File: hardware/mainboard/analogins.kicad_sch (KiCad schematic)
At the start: 27 parts, among them J3 CASTOR PITCH, J4 POLLUX PITCH, J5 CASTOR DUTY, J6 POLLUX DUTY, U6 MCP6004

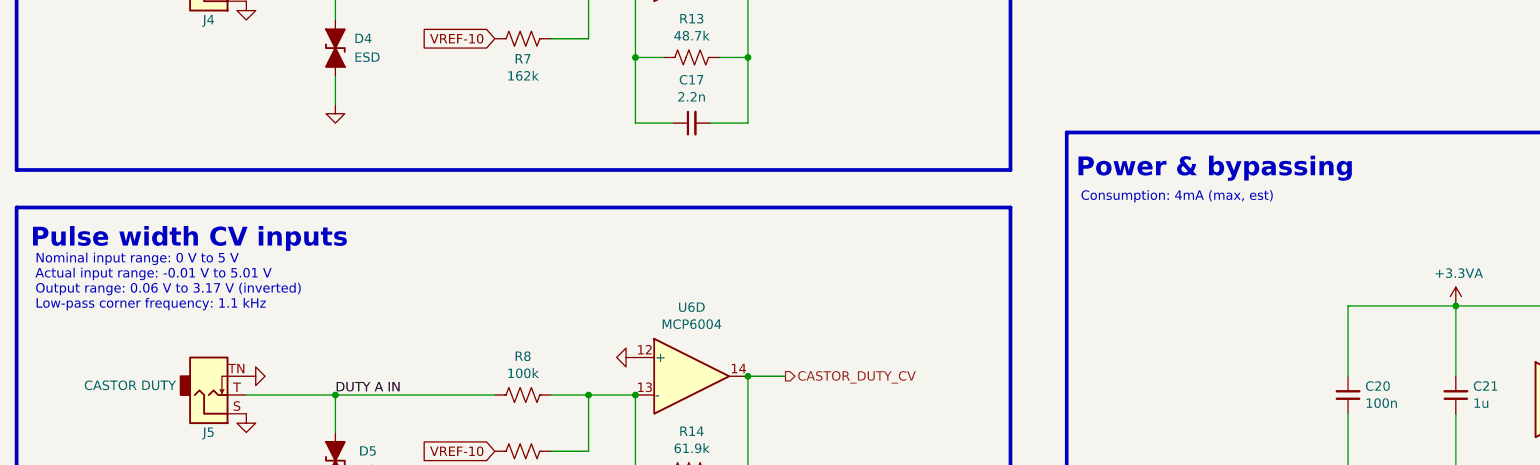
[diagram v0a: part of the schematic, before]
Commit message: A little more schematic cleanup
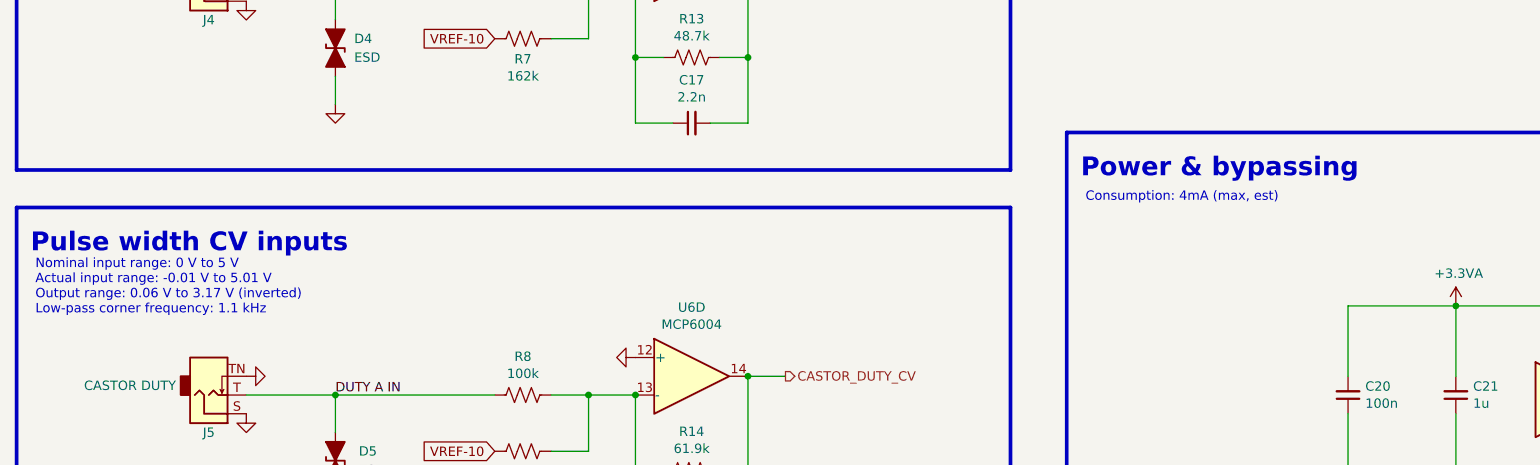
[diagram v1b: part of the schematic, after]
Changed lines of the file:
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@@
     (stroke (width 0) (type default) (color 0 0 0 0))
   )
-  (text "Pulse width CV inputs" (at 19.685 114.935 0)
+  (text "Pulse width CV inputs" (at 19.685 115.57 0)
     (effects (font (size 2.54 2.54) (thickness 0.508) bold) (justify left bottom))
   )
-  (text "Consumption: 4mA (max, est)" (at 161.925 108.585 0)
+  (text "Consumption: 4mA (max, est)" (at 162.56 108.585 0)
     (effects (font (size 1.27 1.27)) (justify left bottom))
   )
-  (text "Power & bypassing" (at 161.29 105.41 0)
+  (text "Power & bypassing" (at 161.925 105.41 0)
     (effects (font (size 2.54 2.54) (thickness 0.508) bold) (justify left bottom))
   )
@@
   )
   (text "Nominal input range: 0 V to 5 V\nActual input range: -0.01 V to 5.01 V\nOutput range: 0.06 V to 3.17 V (inverted)\nLow-pass corner frequency: 1.1 kHz\n"
-    (at 20.32 123.19 0)
+    (at 20.32 123.825 0)
     (effects (font (size 1.27 1.27)) (justify left bottom))
   )

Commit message: Finalize resistor mpns
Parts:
- R10, R4, R6, R8: mpn (none) -> RC0402DR-07100KL
- R11, R9: mpn (none) -> RP73PF1E196KBTD, RK73H1ETTP1963F
- R12, R13: mpn (none) -> RT0402BRD0748K7L
- R14, R15: mpn (none) -> RT0402BRD0761K9L, ERA-2AEB6192X
- R5, R7: mpn (none) -> RP73PF1E162KBTD
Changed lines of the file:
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@@
       (effects (font (size 1.27 1.27)) hide)
     )
-    (property "mpn" "" (id 5) (at 86.36 40.64 0)
+    (property "mpn" "RC0402DR-07100KL" (id 5) (at 86.36 40.64 0)
       (effects (font (size 1.27 1.27)) hide)
     )
@@
       (effects (font (size 1.27 1.27)) hide)
     )
-    (property "mpn" "" (id 5) (at 86.36 48.26 0)
+    (property "mpn" "RP73PF1E162KBTD" (id 5) (at 86.36 48.26 0)
       (effects (font (size 1.27 1.27)) hide)
     )
@@
       (effects (font (size 1.27 1.27)) hide)
     )
-    (property "mpn" "" (id 5) (at 109.22 50.8 0)
+    (property "mpn" "RT0402BRD0748K7L" (id 5) (at 109.22 50.8 0)
       (effects (font (size 1.27 1.27)) hide)
     )
@@
       (effects (font (size 1.27 1.27)) hide)
     )
-    (property "mpn" "" (id 5) (at 86.36 78.74 0)
+    (property "mpn" "RC0402DR-07100KL" (id 5) (at 86.36 78.74 0)
       (effects (font (size 1.27 1.27)) hide)
     )
@@
       (effects (font (size 1.27 1.27)) hide)
     )
-    (property "mpn" "" (id 5) (at 86.36 86.36 0)
+    (property "mpn" "RP73PF1E162KBTD" (id 5) (at 86.36 86.36 0)
       (effects (font (size 1.27 1.27)) hide)
     )
@@
       (effects (font (size 1.27 1.27)) hide)
     )
-    (property "mpn" "" (id 5) (at 109.22 88.9 0)
+    (property "mpn" "RT0402BRD0748K7L" (id 5) (at 109.22 88.9 0)
       (effects (font (size 1.27 1.27)) hide)
     )
@@
       (effects (font (size 1.27 1.27)) hide)
     )
-    (property "mpn" "" (id 5) (at 86.36 134.62 0)
+    (property "mpn" "RC0402DR-07100KL" (id 5) (at 86.36 134.62 0)
       (effects (font (size 1.27 1.27)) hide)
     )
@@
       (effects (font (size 1.27 1.27)) hide)
     )
-    (property "mpn" "" (id 5) (at 86.36 142.24 0)
+    (property "mpn" " RP73PF1E196KBTD, RK73H1ETTP1963F" (id 5) (at 86.36 142.24 0)
       (effects (font (size 1.27 1.27)) hide)
     )
@@
       (effects (font (size 1.27 1.27)) hide)
     )
-    (property "mpn" "" (id 5) (at 109.22 144.78 0)
+    (property "mpn" "RT0402BRD0761K9L,  ERA-2AEB6192X" (id 5) (at 109.22 144.78 0)
       (effects (font (size 1.27 1.27)) hide)
     )
@@
       (effects (font (size 1.27 1.27)) hide)
     )
-    (property "mpn" "" (id 5) (at 86.36 171.45 0)
+    (property "mpn" "RC0402DR-07100KL" (id 5) (at 86.36 171.45 0)
       (effects (font (size 1.27 1.27)) hide)
     )
@@
       (effects (font (size 1.27 1.27)) hide)
     )
-    (property "mpn" "" (id 5) (at 86.36 179.07 0)
+    (property "mpn" " RP73PF1E196KBTD, RK73H1ETTP1963F" (id 5) (at 86.36 179.07 0)
       (effects (font (size 1.27 1.27)) hide)
     )
@@
       (effects (font (size 1.27 1.27)) hide)
     )
-    (property "mpn" "" (id 5) (at 109.22 181.61 0)
-      (effects (font (size 1.27 1.27)) hide)
-    )
+    (property "mpn" "RT0402BRD0761K9L,  ERA-2AEB6192X" (id 5) (at 109.22 181.61 0)
+      (effects (font (size 1.27 1.27)) hide)
+    )

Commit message: Update some MPNs
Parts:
- R11, R9: mpn RP73PF1E196KBTD, RK73H1ETTP1963F -> RP73PF1E196KBTD, RK73H1ETTP1963F
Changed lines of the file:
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@@
       (effects (font (size 1.27 1.27)) hide)
     )
-    (property "mpn" " RP73PF1E196KBTD, RK73H1ETTP1963F" (id 5) (at 86.36 142.24 0)
+    (property "mpn" "RP73PF1E196KBTD, RK73H1ETTP1963F" (id 5) (at 86.36 142.24 0)
       (effects (font (size 1.27 1.27)) hide)
     )
@@
       (effects (font (size 1.27 1.27)) hide)
     )
-    (property "mpn" " RP73PF1E196KBTD, RK73H1ETTP1963F" (id 5) (at 86.36 179.07 0)
+    (property "mpn" "RP73PF1E196KBTD, RK73H1ETTP1963F" (id 5) (at 86.36 179.07 0)
       (effects (font (size 1.27 1.27)) hide)
     )

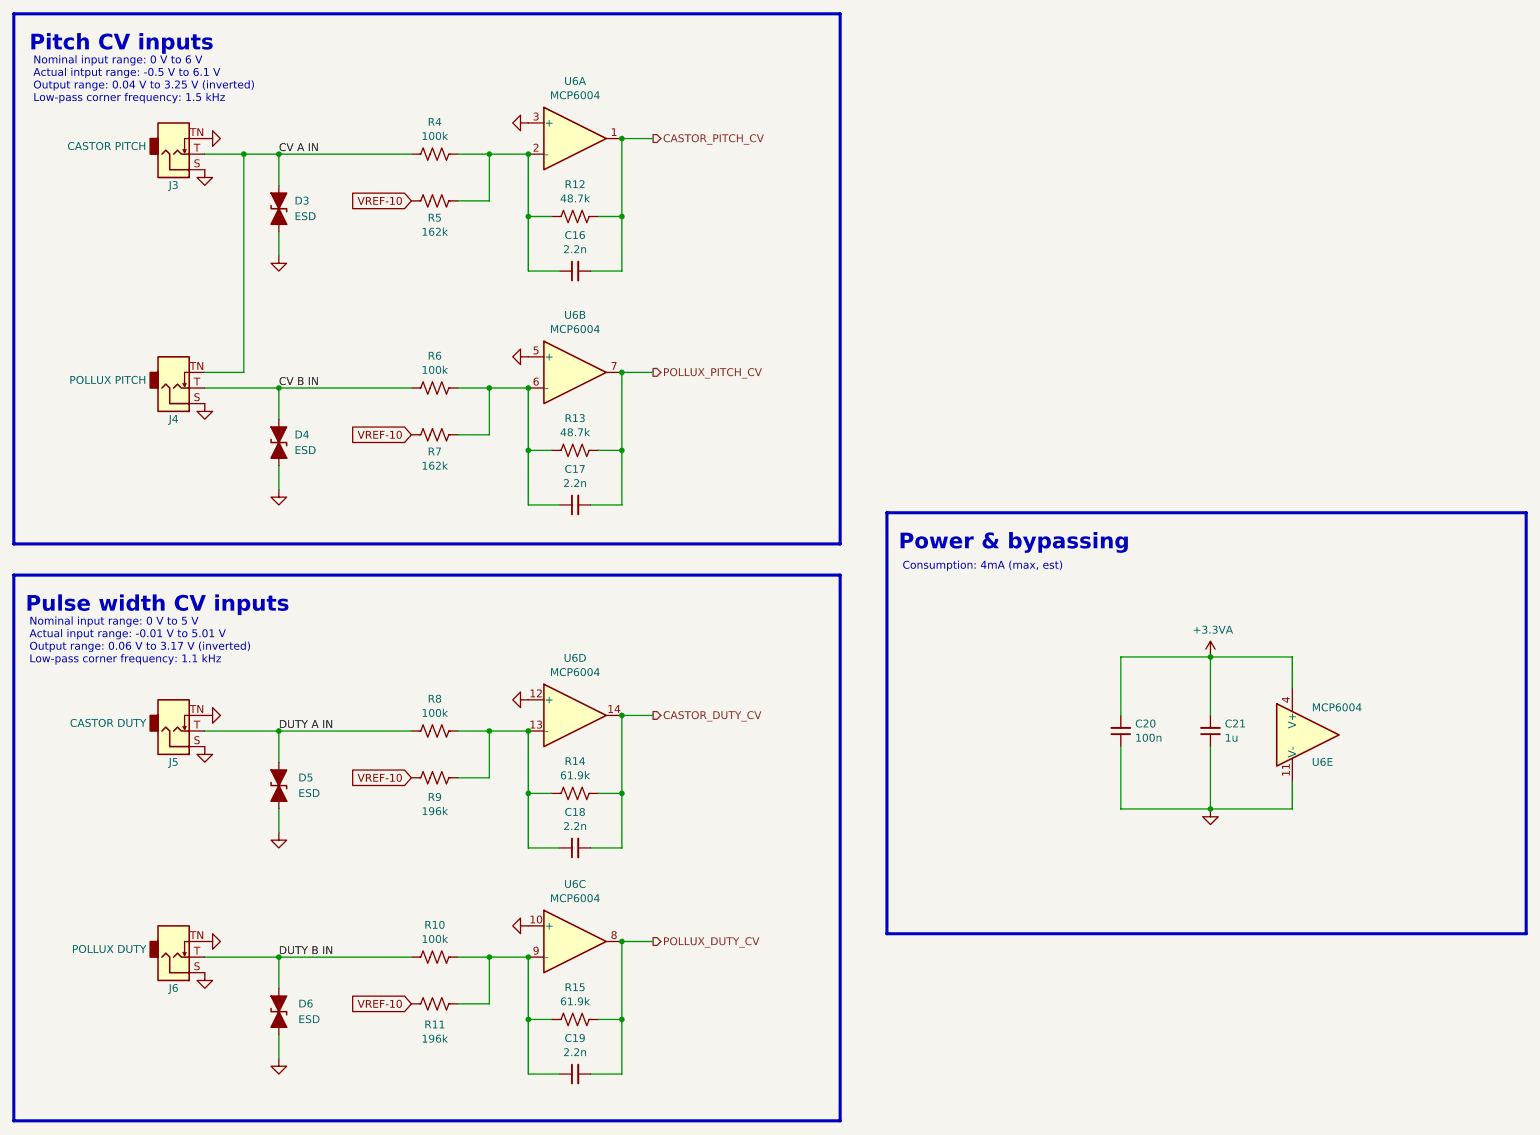
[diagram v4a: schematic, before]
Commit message: hardware: add rating field to schematic
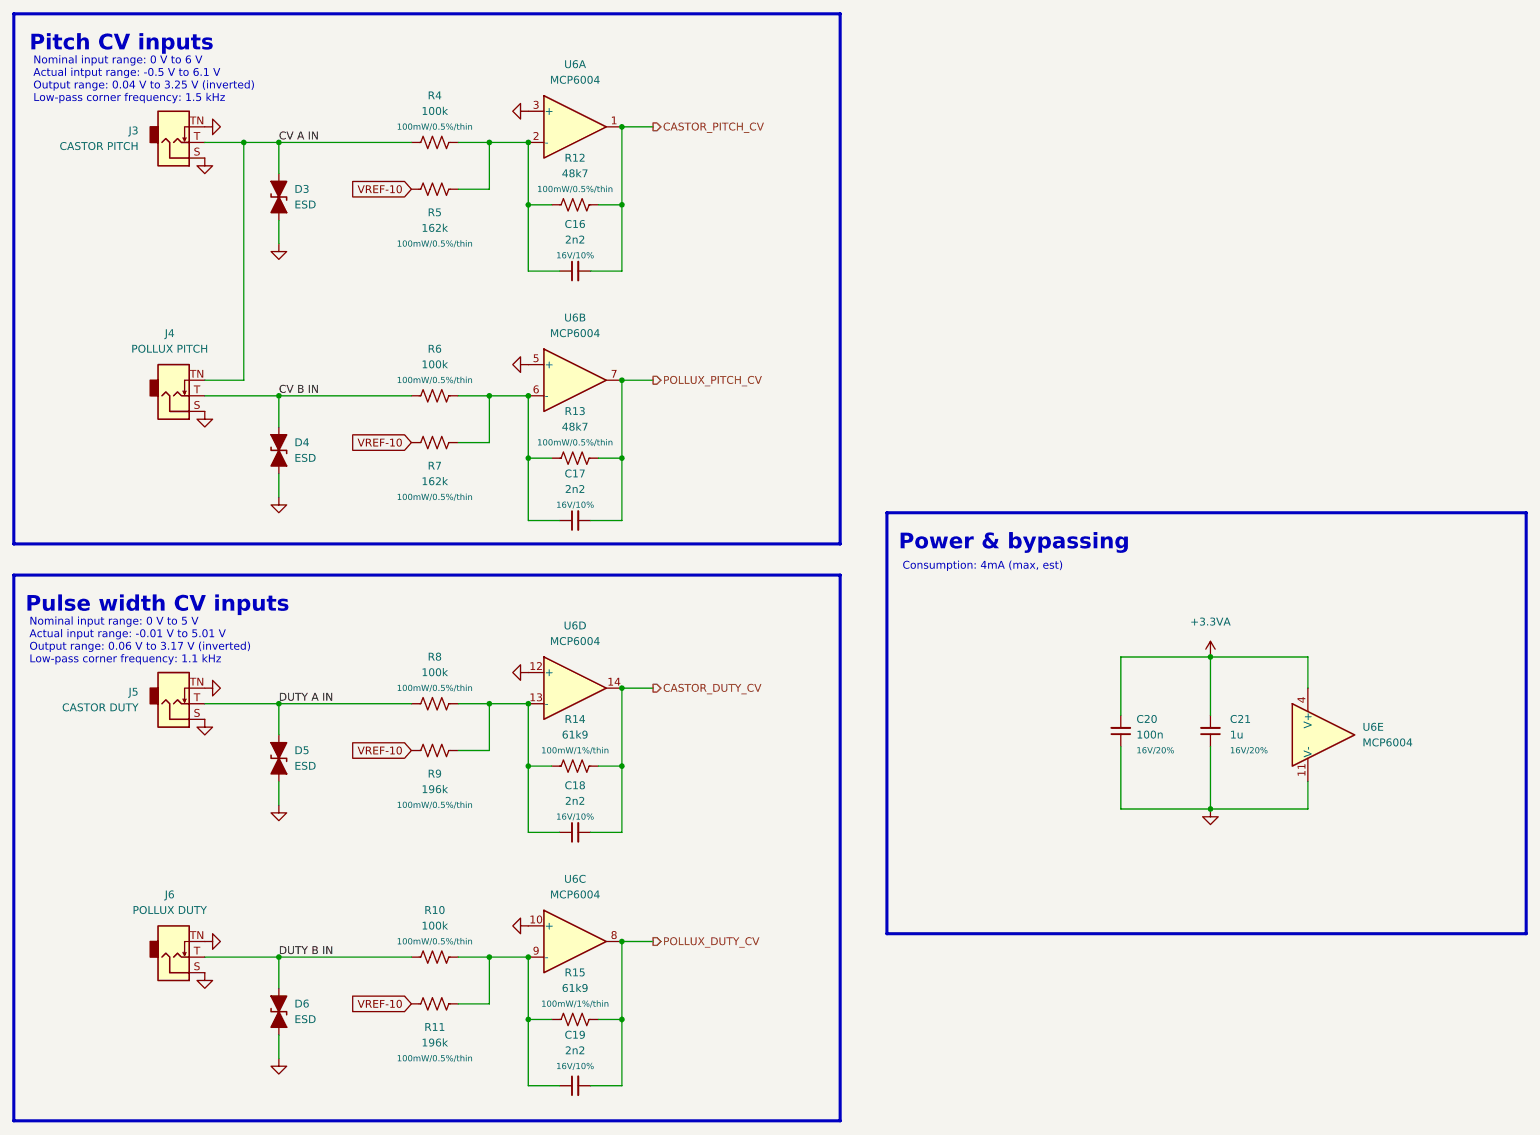
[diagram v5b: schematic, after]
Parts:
- C16, C17, C18, C19: value 2.2n -> 2n2; Rating (none) -> 16V/10%
- C20, C21: Rating (none) -> 16V/20%
- R10, R11, R4, R5, R6, R7, R8, R9: Rating (none) -> 100mW/0.5%/thin
- R12, R13: value 48.7k -> 48k7; Rating (none) -> 100mW/0.5%/thin
- R14, R15: value 61.9k -> 61k9; Rating (none) -> 100mW/1%/thin
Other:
- moved on the sheet: C17, C18, C19, D3, D4, D5, J3, J4, J5, R12, R13, R14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

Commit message: hardware: fixup schematic fields
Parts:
- C16, C17, C18, C19: MPN (none) -> GRM155R71H222KA01D; Notes (none) -> CV filter; Reqs CV filter, 16 V -> (none); finalized yes -> (none); mpn GRM155R71H222KA01D -> (none)
- C20: MPN (none) -> CL05B104KO5NNNC; MacroFab MPN (none) -> MF-CAP-0402-0.1uF; Notes (none) -> Bypass; Reqs Bypass, 16 V -> (none); finalized yes -> (none); macrofab_mpn MF-CAP-0402-0.1uF -> (none); mpn CL05B104KO5NNNC -> (none)
- C21: MPN (none) -> CL05A105KO5NNNC; MacroFab MPN (none) -> MF-CAP-0402-1uF; Notes (none) -> Bypass; Reqs Bypass, 16 V -> (none); finalized yes -> (none); macrofab_mpn MF-CAP-0402-1uF -> (none); mpn CL05A105KO5NNNC -> (none)
- D3, D4, D5, D6: MPN (none) -> B72500T0250K060; Notes (none) -> ESD diode, ceradiode, MOV, or small capacitor; Reqs ESD diode, ceradiode, MOV, or small capacitor -> (none); finalized yes -> (none); mpn B72500T0250K060 -> (none)
- J3, J4, J5, J6: MPN (none) -> WQP-WQP518MA; finalized yes -> (none); mpn WQP-WQP518MA -> (none)
- R10, R4, R6, R8: MPN (none) -> RC0402DR-07100KL; Notes (none) -> Low frequency analog input; Reqs Analog input, 0.5%, 100 mW, thin film -> (none); mpn RC0402DR-07100KL -> (none)
- R11, R9: MPN (none) -> RP73PF1E196KBTD, RK73H1ETTP1963F; Notes (none) -> Low frequency analog input; Reqs Analog input, 0.5%, 100 mW, thin film -> (none); mpn RP73PF1E196KBTD, RK73H1ETTP1963F -> (none)
- R12, R13: MPN (none) -> RT0402BRD0748K7L; Notes (none) -> Low frequency analog input; Reqs Analog input, 0.5%, 100 mW, thin film -> (none); mpn RT0402BRD0748K7L -> (none)
- R14, R15: MPN (none) -> RT0402BRD0761K9L, ERA-2AEB6192X; Notes (none) -> Low frequency analog input; Reqs Analog input, 1%, 100 mW, thin film -> (none); mpn RT0402BRD0761K9L, ERA-2AEB6192X -> (none)
- R5, R7: MPN (none) -> RP73PF1E162KBTD; Notes (none) -> Low frequency analog input; Reqs Analog input, 0.5%, 100 mW, thin film -> (none); mpn RP73PF1E162KBTD -> (none)
- U6: MPN (none) -> MCP6004T-I/ST, MCP6004T-E/ST; finalized yes -> (none); mpn MCP6004T-I/ST, MCP6004T-E/ST -> (none)
